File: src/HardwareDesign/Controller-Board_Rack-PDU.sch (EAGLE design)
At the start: 144 parts, among them IC1 W5500, IC2 RP2040, IC3 MCP6001AIDBVRG, IC4 W25Q128JVPIQ, IC5 MP2315S, IC6 CAT24C256HU4IGT3, IC7 MP2315GJ-Z, IC8 MCP23S18-E/MJ, SW3 TP, SW5 TP, X1 XC53M4-25.000-F18NJDTL, X2 K5A1200015304P

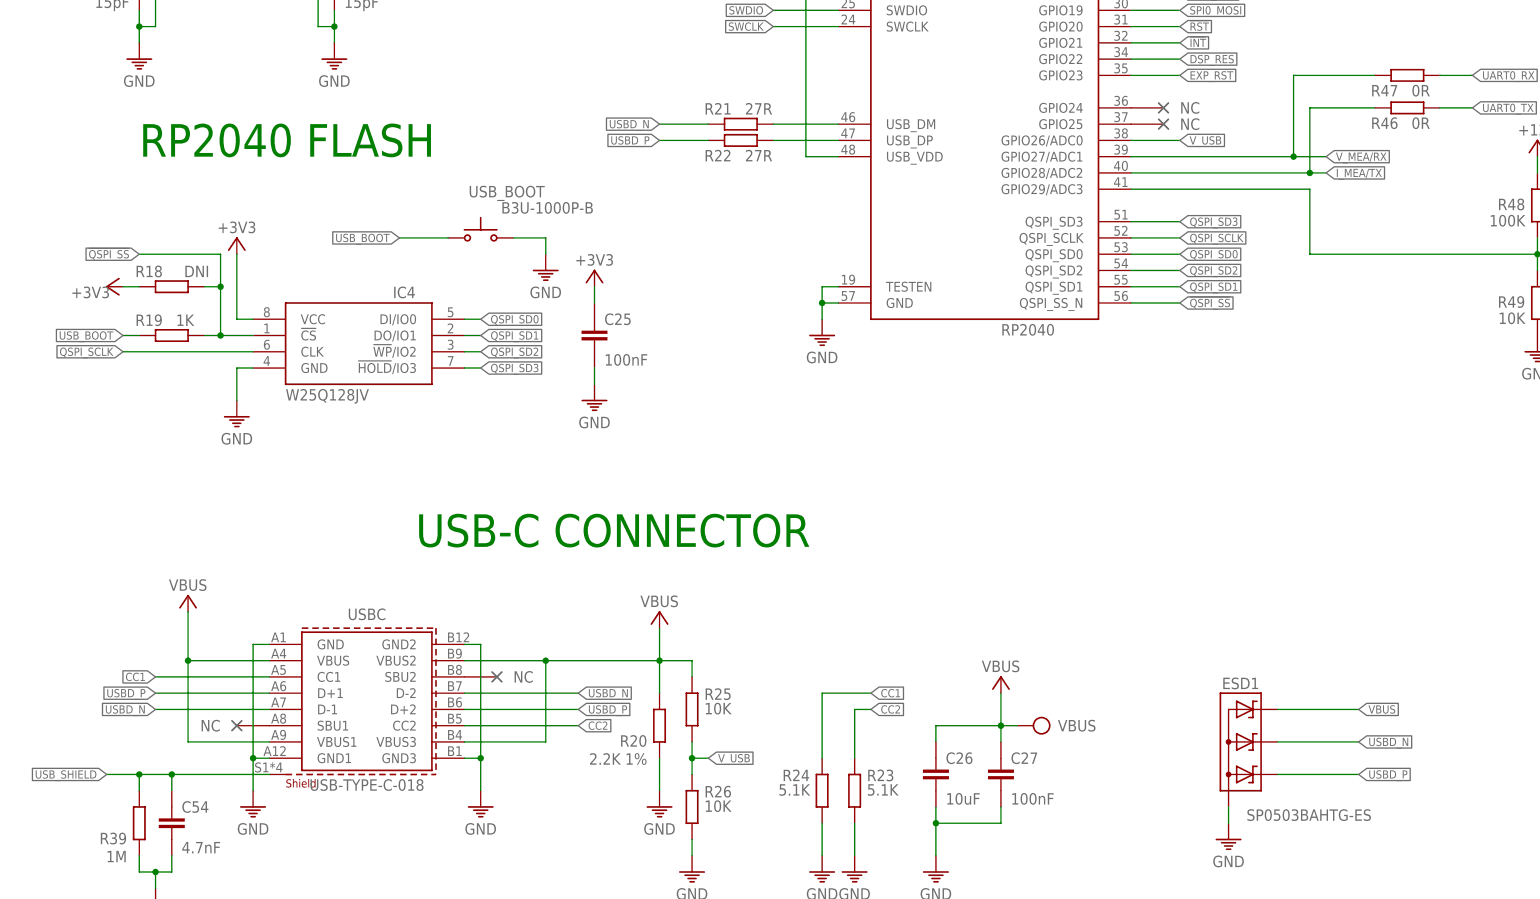
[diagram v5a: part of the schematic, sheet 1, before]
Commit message: add DiffPairCheck to repo. Update Controller-boart to rev1.1
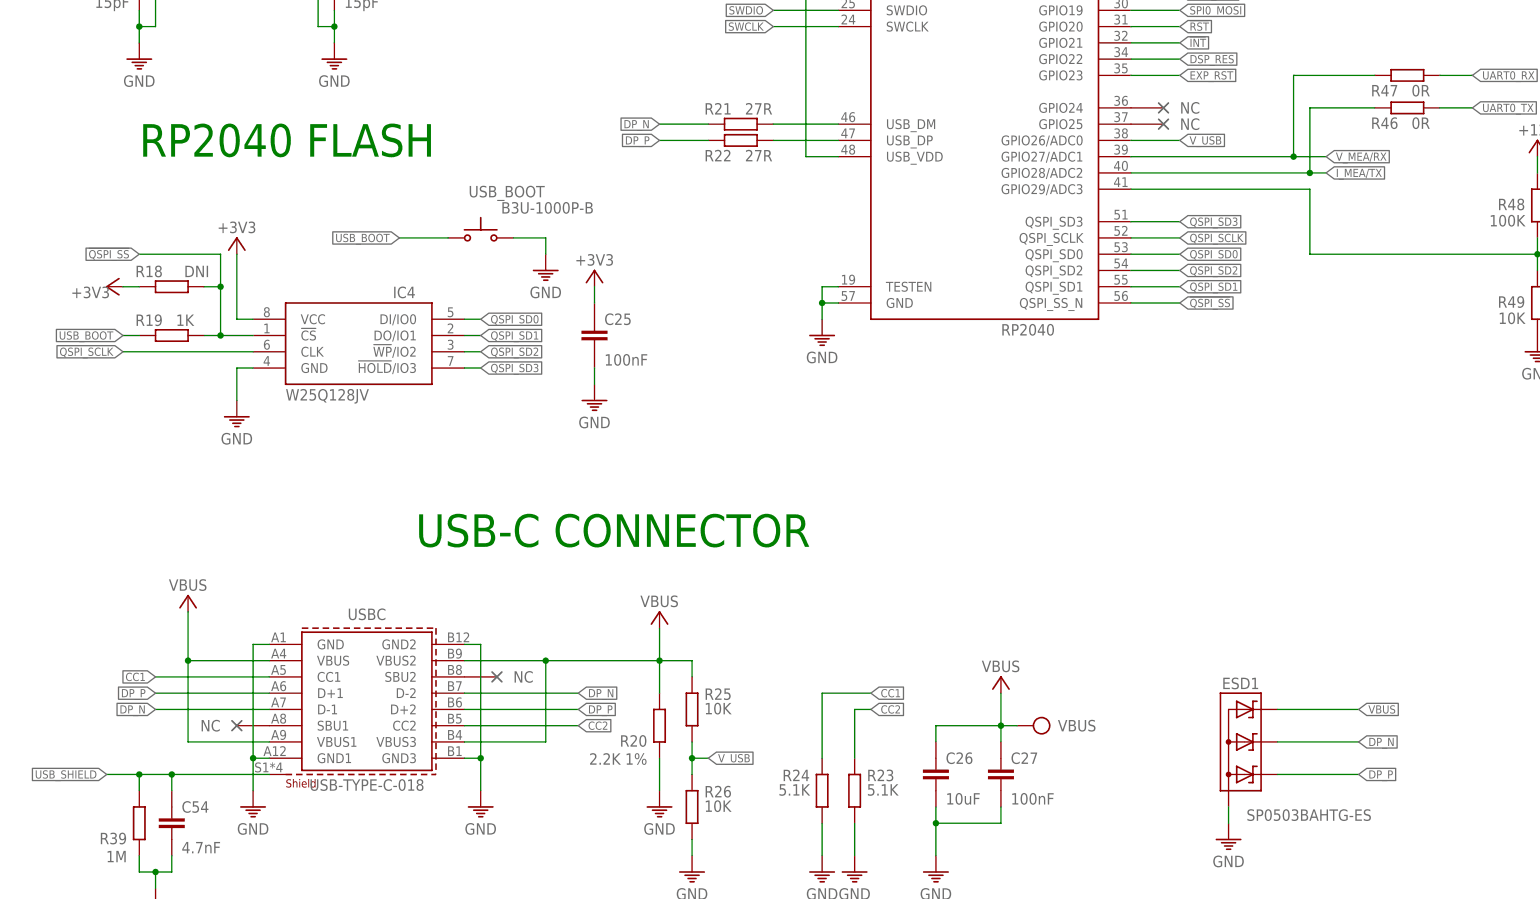
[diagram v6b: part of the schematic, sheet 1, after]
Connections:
- net RDC_N renamed RDC_RD_N
- net RDC_P renamed RDC_RD_P
- net RP_USBD_N renamed USB_DP_N
- net RP_USBD_P renamed USB_DP_P
- net RX_N renamed RX_RD_N
- net RX_P renamed RX_RD_P
- net TX_N renamed TX_TD_N
- net TX_P renamed TX_TD_P
- net USBD_N renamed DP_N
- net USBD_P renamed DP_P
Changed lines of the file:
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@@
 </segment>
 </net>
-<net name="RP_USBD_N" class="2">
+<net name="USB_DP_N" class="2">
 <segment>
 <pinref part="IC2" gate="G$1" pin="USB_DM"/>
@@
 </segment>
 </net>
-<net name="RP_USBD_P" class="2">
+<net name="USB_DP_P" class="2">
 <segment>
 <pinref part="IC2" gate="G$1" pin="USB_DP"/>
@@
 </segment>
 </net>
-<net name="USBD_N" class="2">
+<net name="DP_N" class="2">
 <segment>
 <pinref part="R21" gate="G$1" pin="1"/>
@@
 </segment>
 </net>
-<net name="USBD_P" class="2">
+<net name="DP_P" class="2">
 <segment>
 <pinref part="R22" gate="G$1" pin="1"/>
@@
 </segment>
 </net>
-<net name="TX_N" class="1">
+<net name="TX_TD_N" class="1">
 <segment>
 <pinref part="IC1" gate="G$1" pin="TXN"/>
 <wire x1="137.16" y1="195.58" x2="124.46" y2="195.58" width="0.1524" layer="91"/>
 <pinref part="R1" gate="G$1" pin="1"/>
-<label x="129.54" y="195.58" size="1.778" layer="95"/>
-</segment>
-</net>
-<net name="TX_P" class="1">
+<label x="127" y="195.58" size="1.778" layer="95"/>
+</segment>
+</net>
+<net name="TX_TD_P" class="1">
 <segment>
 <pinref part="IC1" gate="G$1" pin="TXP"/>
 <pinref part="R2" gate="G$1" pin="1"/>
 <wire x1="137.16" y1="193.04" x2="124.46" y2="193.04" width="0.1524" layer="91"/>
-<label x="129.54" y="193.04" size="1.778" layer="95"/>
-</segment>
-</net>
-<net name="RX_N" class="1">
+<label x="127" y="193.04" size="1.778" layer="95"/>
+</segment>
+</net>
+<net name="RX_RD_N" class="1">
 <segment>
 <pinref part="IC1" gate="G$1" pin="RXN"/>
 <pinref part="R4" gate="G$1" pin="1"/>
 <wire x1="124.46" y1="187.96" x2="147.32" y2="187.96" width="0.1524" layer="91"/>
-<label x="129.54" y="187.96" size="1.778" layer="95"/>
-</segment>
-</net>
-<net name="RX_P" class="1">
+<label x="127" y="187.96" size="1.778" layer="95"/>
+</segment>
+</net>
+<net name="RX_RD_P" class="1">
 <segment>
 <pinref part="IC1" gate="G$1" pin="RXP"/>
 <pinref part="R3" gate="G$1" pin="1"/>
 <wire x1="124.46" y1="185.42" x2="147.32" y2="185.42" width="0.1524" layer="91"/>
-<label x="129.54" y="185.42" size="1.778" layer="95"/>
+<label x="127" y="185.42" size="1.778" layer="95"/>
 </segment>
 </net>
@@
 </segment>
 </net>
-<net name="RDC_N" class="1">
+<net name="RDC_RD_N" class="1">
 <segment>
 <pinref part="R4" gate="G$1" pin="2"/>
@@
 <junction x="162.56" y="187.96"/>
 <pinref part="C3" gate="G$1" pin="1"/>
-</segment>
-</net>
-<net name="RDC_P" class="1">
+<label x="162.56" y="187.96" size="1.27" layer="95"/>
+</segment>
+</net>
+<net name="RDC_RD_P" class="1">
 <segment>
 <pinref part="R3" gate="G$1" pin="2"/>
@@
 <junction x="167.64" y="185.42"/>
 <pinref part="C4" gate="G$1" pin="1"/>
-</segment>
-</net>
+<label x="162.56" y="185.42" size="1.27" layer="95"/>
+</segment>
+</net>
